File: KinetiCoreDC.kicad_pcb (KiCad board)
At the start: 2 copper layers, 69 parts, among them Q1 BSN20, Q2 BSN20, U1 STM32G070KBT6, U10 MCP1703Ax-330xxDB, U11 WE-TVS-82400102, U2 SN74LVC2G14DBV, U3 DRV8874PWPR, U6 THVD1400D, U7 TLP2310, U8 TLP2310, U9 LTC4365TS8

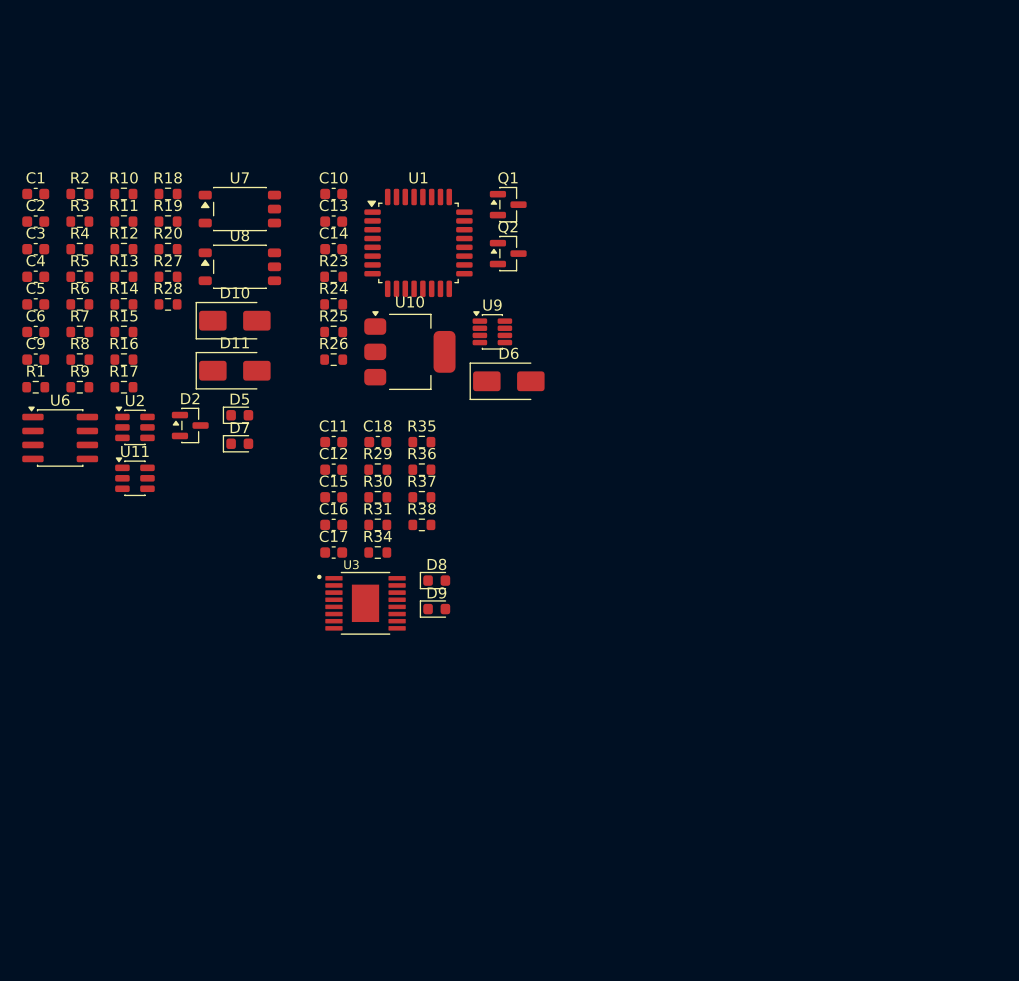
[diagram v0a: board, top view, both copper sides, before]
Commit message: feat : add SMLVN6RGB status LED stage with balanced 3.3V ballast resistors
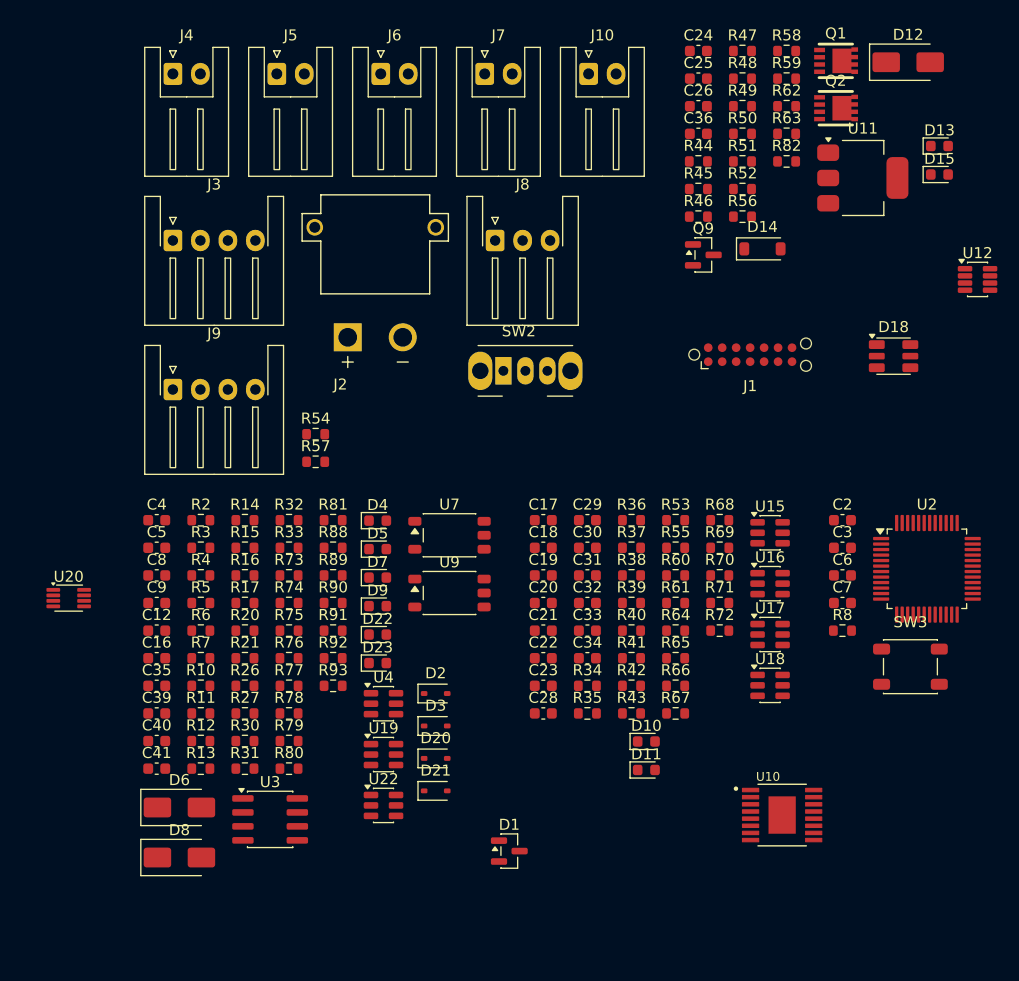
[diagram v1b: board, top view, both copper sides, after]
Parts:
- removed C1, C10, C15: 100nF, Capacitor_SMD:C_0603_1608Metric
- removed C11: 22nF, Capacitor_SMD:C_0603_1608Metric
- removed C13, C14: 1uF, Capacitor_SMD:C_0603_1608Metric
- removed R1, R18, R19, R28: 100R, Resistor_SMD:R_0603_1608Metric
- removed R23: 100k, Resistor_SMD:R_0603_1608Metric
- removed R24: 1.2M, Resistor_SMD:R_0603_1608Metric
- removed R25: 150K, Resistor_SMD:R_0603_1608Metric
- removed R29: 500R, Resistor_SMD:R_0603_1608Metric
- removed R9: 2.2K, Resistor_SMD:R_0603_1608Metric
- removed U1: STM32G070KBT6, Package_QFP:LQFP-32_7x7mm_P0.8mm
- removed U6: THVD1400D, Package_SO:SOIC-8_3.9x4.9mm_P1.27mm
- removed U8: TLP2310, Package_SO:SO-5-6_4.55x3.7mm_P1.27mm
- added C19: 22nF, Capacitor_SMD:C_0603_1608Metric, F.Cu at (160.7, 93.4)
- added C20: 4.7uF, Capacitor_SMD:C_0603_1608Metric, F.Cu at (160.7, 95.9)
- added C21: 22uF, Capacitor_SMD:C_0603_1608Metric, F.Cu at (160.7, 98.5)
- added C22: 100nF, Capacitor_SMD:C_0603_1608Metric, F.Cu at (160.7, 101.0)
- added C23: 10nF, Capacitor_SMD:C_0603_1608Metric, F.Cu at (160.7, 103.5)
- added C24: 1uF, Capacitor_SMD:C_0603_1608Metric, F.Cu at (174.8, 45.8)
- added C25: 1uF, Capacitor_SMD:C_0603_1608Metric, F.Cu at (174.8, 48.3)
- added C26: 100nF, Capacitor_SMD:C_0603_1608Metric, F.Cu at (174.8, 50.8)
- added C28: 1nF, Capacitor_SMD:C_0603_1608Metric, F.Cu at (160.7, 106.0)
- added C29: 1nF, Capacitor_SMD:C_0603_1608Metric, F.Cu at (164.7, 88.4)
- added C30: 100nF, Capacitor_SMD:C_0603_1608Metric, F.Cu at (164.7, 90.9)
- added C31: 100nF, Capacitor_SMD:C_0603_1608Metric, F.Cu at (164.7, 93.4)
- added C32: 100nF, Capacitor_SMD:C_0603_1608Metric, F.Cu at (164.7, 95.9)
- added C33: 100nF, Capacitor_SMD:C_0603_1608Metric, F.Cu at (164.7, 98.5)
- added C34: 100nF, Capacitor_SMD:C_0603_1608Metric, F.Cu at (164.7, 101.0)
- added C35: 220nF, Capacitor_SMD:C_0603_1608Metric, F.Cu at (125.5, 103.5)
- added C36: 1uF, Capacitor_SMD:C_0603_1608Metric, F.Cu at (174.8, 53.3)
- added C39: 10nF, Capacitor_SMD:C_0603_1608Metric, F.Cu at (125.5, 106.0)
- added C40: 10nF, Capacitor_SMD:C_0603_1608Metric, F.Cu at (125.5, 108.5)
- added C41: 100nF, Capacitor_SMD:C_0603_1608Metric, F.Cu at (125.5, 111.0)
- added C7: 100nF, Capacitor_SMD:C_0603_1608Metric, F.Cu at (187.9, 95.9)
- added C8: 100nF, Capacitor_SMD:C_0603_1608Metric, F.Cu at (125.5, 93.4)
- added D1: SM712, Package_TO_SOT_SMD:SOT-23, F.Cu at (157.6, 118.5)
- added D12: SMBJ15CA, Diode_SMD:D_SMA, F.Cu at (193.8, 46.8)
- added D13: LED_Small, LED_SMD:LED_0603_1608Metric, F.Cu at (196.7, 54.4)
- added D14: NSI45020A, Diode_SMD:D_SOD-123, F.Cu at (180.6, 63.7)
- added D15: LED_Small, LED_SMD:LED_0603_1608Metric, F.Cu at (196.7, 57.0)
- added D18: SMLVN6RGB, LED_SMD:LED_ROHM_SMLVN6, F.Cu at (192.5, 73.5)
- added D20: 1N4148WS, Diode_SMD:D_SOD-323, F.Cu at (150.9, 110.1)
- added D21: 1N4148WS, Diode_SMD:D_SOD-323, F.Cu at (150.9, 113.0)
- added D22: LED_Small, LED_SMD:LED_0603_1608Metric, F.Cu at (145.6, 98.8)
- added D23: LED_Small, LED_SMD:LED_0603_1608Metric, F.Cu at (145.6, 101.4)
- added D3: 1N4148WS, Diode_SMD:D_SOD-323, F.Cu at (150.9, 107.1)
- added D4: LED_Small, LED_SMD:LED_0603_1608Metric, F.Cu at (145.6, 88.5)
- added J1: TC2070-IDC-NL, KineticCore:Tag-Connect_TC2070-IDC-FP_2x07_P1.27mm_Vertical, F.Cu at (179.5, 73.4)
- added J10: JST_XH_S2B-A, Connector_JST:JST_XH_S2B-XH-A_1x02_P2.50mm_Horizontal, F.Cu at (164.8, 47.8)
- added J2: XT30PW-M, KineticCore:AMASS_XT30PW-M, F.Cu at (145.4, 61.8)
- added J3: JST_XH_S4B-A, Connector_JST:JST_XH_S4B-XH-A-1_1x04_P2.50mm_Horizontal, F.Cu at (127.0, 63.0)
- added J4: JST_XH_S2B-A, Connector_JST:JST_XH_S2B-XH-A_1x02_P2.50mm_Horizontal, F.Cu at (127.0, 47.8)
- added J5: JST_XH_S2B-A, Connector_JST:JST_XH_S2B-XH-A_1x02_P2.50mm_Horizontal, F.Cu at (136.4, 47.8)
- added J6: JST_XH_S2B-A, Connector_JST:JST_XH_S2B-XH-A_1x02_P2.50mm_Horizontal, F.Cu at (145.9, 47.8)
- added J7: JST_XH_S2B-A, Connector_JST:JST_XH_S2B-XH-A_1x02_P2.50mm_Horizontal, F.Cu at (155.3, 47.8)
- added J8: JST_XH_S3B, Connector_JST:JST_XH_S3B-XH-A-1_1x03_P2.50mm_Horizontal, F.Cu at (156.3, 63.0)
- added J9: JST_XH_S4B-A, Connector_JST:JST_XH_S4B-XH-A-1_1x04_P2.50mm_Horizontal, F.Cu at (127.0, 76.5)
- added Q9: BSS84, Package_TO_SOT_SMD:SOT-23, F.Cu at (175.2, 64.3)
- added R21: 330R, Resistor_SMD:R_0603_1608Metric, F.Cu at (133.5, 101.0)
- added R32: 470R, Resistor_SMD:R_0603_1608Metric, F.Cu at (137.5, 88.4)
- added R33: 22R, Resistor_SMD:R_0603_1608Metric, F.Cu at (137.5, 90.9)
- added R39: 47K, Resistor_SMD:R_0603_1608Metric, F.Cu at (168.7, 95.9)
- added R40: 10K, Resistor_SMD:R_0603_1608Metric, F.Cu at (168.7, 98.5)
- added R41: 2.49K, Resistor_SMD:R_0603_1608Metric, F.Cu at (168.7, 101.0)
- added R42: 22R, Resistor_SMD:R_0603_1608Metric, F.Cu at (168.7, 103.5)
- added R43: 1K, Resistor_SMD:R_0603_1608Metric, F.Cu at (168.7, 106.0)
- added R44: 2.7M, Resistor_SMD:R_0603_1608Metric, F.Cu at (174.8, 55.8)
- added R45: 150k, Resistor_SMD:R_0603_1608Metric, F.Cu at (174.8, 58.3)
- added R46: 100k, Resistor_SMD:R_0603_1608Metric, F.Cu at (174.8, 60.8)
- added R47: 510k, Resistor_SMD:R_0603_1608Metric, F.Cu at (178.8, 45.8)
- added R48: 470R, Resistor_SMD:R_0603_1608Metric, F.Cu at (178.8, 48.3)
- added R49: 10R, Resistor_SMD:R_0603_1608Metric, F.Cu at (178.8, 50.8)
- added R50: 10R, Resistor_SMD:R_0603_1608Metric, F.Cu at (178.8, 53.3)
- added R51: 100R, Resistor_SMD:R_0603_1608Metric, F.Cu at (178.8, 55.8)
- added R52: 100R, Resistor_SMD:R_0603_1608Metric, F.Cu at (178.8, 58.3)
- added R53: 22R, Resistor_SMD:R_0603_1608Metric, F.Cu at (172.7, 88.4)
- added R54: 22R, Resistor_SMD:R_0603_1608Metric, F.Cu at (140.0, 80.6)
- added R55: 1K, Resistor_SMD:R_0603_1608Metric, F.Cu at (172.7, 90.9)
- added R56: 20k, Resistor_SMD:R_0603_1608Metric, F.Cu at (178.8, 60.8)
- added R57: 22R, Resistor_SMD:R_0603_1608Metric, F.Cu at (140.0, 83.1)
- added R58: 10k, Resistor_SMD:R_0603_1608Metric, F.Cu at (182.8, 45.8)
- added R59: 100k, Resistor_SMD:R_0603_1608Metric, F.Cu at (182.8, 48.3)
- added R60: 22R, Resistor_SMD:R_0603_1608Metric, F.Cu at (172.7, 93.4)
- added R61: 22R, Resistor_SMD:R_0603_1608Metric, F.Cu at (172.7, 95.9)
- added R62: 330R, Resistor_SMD:R_0603_1608Metric, F.Cu at (182.8, 50.8)
- added R63: 180R, Resistor_SMD:R_0603_1608Metric, F.Cu at (182.8, 53.3)
- added R64: 1K, Resistor_SMD:R_0603_1608Metric, F.Cu at (172.7, 98.5)
- added R65: 100R, Resistor_SMD:R_0603_1608Metric, F.Cu at (172.7, 101.0)
- added R66: 100R, Resistor_SMD:R_0603_1608Metric, F.Cu at (172.7, 103.5)
- added R67: 2.2K, Resistor_SMD:R_0603_1608Metric, F.Cu at (172.7, 106.0)
- added R68: 2.2K, Resistor_SMD:R_0603_1608Metric, F.Cu at (176.7, 88.4)
- added R69: 10K, Resistor_SMD:R_0603_1608Metric, F.Cu at (176.7, 90.9)
- added R70: 10K, Resistor_SMD:R_0603_1608Metric, F.Cu at (176.7, 93.4)
- added R71: 100R, Resistor_SMD:R_0603_1608Metric, F.Cu at (176.7, 95.9)
- added R72: 100R, Resistor_SMD:R_0603_1608Metric, F.Cu at (176.7, 98.5)
- added R73: 22R, Resistor_SMD:R_0603_1608Metric, F.Cu at (137.5, 93.4)
- added R74: 22R, Resistor_SMD:R_0603_1608Metric, F.Cu at (137.5, 95.9)
- added R75: 10K, Resistor_SMD:R_0603_1608Metric, F.Cu at (137.5, 98.5)
- added R76: 22R, Resistor_SMD:R_0603_1608Metric, F.Cu at (137.5, 101.0)
- added R77: 22R, Resistor_SMD:R_0603_1608Metric, F.Cu at (137.5, 103.5)
- added R78: 10K, Resistor_SMD:R_0603_1608Metric, F.Cu at (137.5, 106.0)
- added R79: 10K, Resistor_SMD:R_0603_1608Metric, F.Cu at (137.5, 108.5)
- added R80: 22R, Resistor_SMD:R_0603_1608Metric, F.Cu at (137.5, 111.0)
- added R81: 22R, Resistor_SMD:R_0603_1608Metric, F.Cu at (141.5, 88.4)
- added R82: 180R, Resistor_SMD:R_0603_1608Metric, F.Cu at (182.8, 55.8)
- added R88: 1K, Resistor_SMD:R_0603_1608Metric, F.Cu at (141.5, 90.9)
- added R89: 1K, Resistor_SMD:R_0603_1608Metric, F.Cu at (141.5, 93.4)
- added R90: 1M, Resistor_SMD:R_0603_1608Metric, F.Cu at (141.5, 95.9)
- added R91: 1M, Resistor_SMD:R_0603_1608Metric, F.Cu at (141.5, 98.5)
- added R92: 470R, Resistor_SMD:R_0603_1608Metric, F.Cu at (141.5, 101.0)
- added R93: 470R, Resistor_SMD:R_0603_1608Metric, F.Cu at (141.5, 103.5)
- added SW2: OS102011MA1Q, Button_Switch_THT:SW_Slide_SPDT_Angled_CK_OS102011MA1Q, F.Cu at (157.0, 74.8)
- added SW3: PTS647, Button_Switch_SMD:SW_SPST_PTS647_Sx38, F.Cu at (194.0, 101.7)
- added U12: LTC4365TS8, Package_TO_SOT_SMD:TSOT-23-8, F.Cu at (200.1, 66.5)
- added U15: WE-TVS-82400102, Package_TO_SOT_SMD:SOT-23-6, F.Cu at (181.3, 89.6)
- added U16: SN74LVC2G14DBV, Package_TO_SOT_SMD:SOT-23-6, F.Cu at (181.3, 94.2)
- added U17: WE-TVS-82400102, Package_TO_SOT_SMD:SOT-23-6, F.Cu at (181.3, 98.8)
- added U18: SN74LVC2G14DBV, Package_TO_SOT_SMD:SOT-23-6, F.Cu at (181.3, 103.4)
- added U19: WE-TVS-82400102, Package_TO_SOT_SMD:SOT-23-6, F.Cu at (146.1, 109.7)
- added U20: 74LVC2G126, Package_SO:VSSOP-8_2.3x2mm_P0.5mm, F.Cu at (117.5, 95.5)
- added U22: SN74LVC2G14DBV, Package_TO_SOT_SMD:SOT-23-6, F.Cu at (146.1, 114.3)
- added U4: SN74LVC2G14DBV, Package_TO_SOT_SMD:SOT-23-6, F.Cu at (146.1, 105.1)
- C17: value 4.7uF -> 100nF
- C18: value 22uF -> 100nF
- C3: value 100nF -> 4.7uF
- C4, C5: value 100nF -> 10nF
- D10, D11: value SMAJ5.0A -> LED_Small; footprint Diode_SMD:D_SMA -> LED_SMD:LED_0603_1608Metric
- D2: value SM712 -> 1N4148WS; footprint Package_TO_SOT_SMD:SOT-23 -> Diode_SMD:D_SOD-323
- D6: value SMAJ15CA -> SMAJ6.0A
- D8: value LED_Small -> SMAJ6.0A; footprint LED_SMD:LED_0603_1608Metric -> Diode_SMD:D_SMA
- Q1, Q2: value BSN20 -> SIS412DN-T1-GE3; footprint Package_TO_SOT_SMD:SOT-23 -> KineticCore:POWERPAK-1212-8
- R10: value 2.2K -> 1M
- R11, R12: value 100R -> 10K
- R15, R16: value 10R -> 22R
- R17: value 120R -> 22R
- R2: value 470R -> 120R
- R20, R31: value 10K -> 330R
- R26: value 150k -> 470R
- R27: value 10K -> 22R
- R30: value 500R -> 330R
- R34: value 2.49K -> 22R
- R35: value 0R -> 2K
- R37: value 16k -> 15K
- R38: value 50k -> 0R
- R4: value 470R -> 1K
- R5: value 1K -> 10R
- R6: value 100R -> 10R
- R7: value 10K -> 1M
- R8: value 10K -> 100R
- U10: value MCP1703Ax-330xxDB -> DRV8874PWPR; footprint Package_TO_SOT_SMD:SOT-223-3_TabPin2 -> KineticCore:SOP65P640X120-17N
- U11: value WE-TVS-82400102 -> MCP1703Ax-330xxDB; footprint Package_TO_SOT_SMD:SOT-23-6 -> Package_TO_SOT_SMD:SOT-223-3_TabPin2
- U2: value SN74LVC2G14DBV -> STM32G070CBTx; footprint Package_TO_SOT_SMD:SOT-23-6 -> Package_QFP:LQFP-48_7x7mm_P0.5mm
- U3: value DRV8874PWPR -> THVD1400D; footprint KineticCore:SOP65P640X120-17N -> Package_SO:SOIC-8_3.9x4.9mm_P1.27mm
- U9: value LTC4365TS8 -> TLP2310; footprint Package_TO_SOT_SMD:TSOT-23-8 -> Package_SO:SO-5-6_4.55x3.7mm_P1.27mm
- moved C2 78.2 mm to (187.9, 88.4)
- moved C3 78.2 mm to (187.9, 90.9)
- moved C6 76.6 mm to (187.9, 93.4)
- moved R8 73.6 mm to (187.9, 98.5)
- moved U2 73.1 mm to (195.5, 92.8)
- moved U11 71.6 mm to (189.7, 57.3)
- moved U10 54.0 mm to (182.4, 115.2)
- moved D10 53.5 mm to (170.0, 108.5)
- moved D11 52.1 mm to (170.0, 111.1)
- moved D6 49.0 mm to (127.6, 114.5)
- moved R12 45.3 mm to (129.5, 108.5)
- moved R11 45.3 mm to (129.5, 106.0)
- moved R13 45.3 mm to (129.5, 111.0)
- moved R10 45.3 mm to (129.5, 103.5)
- moved R27 40.3 mm to (133.5, 106.0)
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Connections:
- C12 pad 1: Net-(U3-VCP) -> +3V3
- C12 pad 2: VM -> GND
- C16 pad 1: VM -> +3V3
- C2 pad 1: +3.3V -> +3V3
- C4 pad 1: +3V3 -> GND
- C4 pad 2: GND -> Net-(D3-A)
- C5 pad 2: Net-(U2-2A) -> Net-(D2-A)
- C6 pad 1: GND -> Net-(U2-NRST)
- C6 pad 2: Net-(U2-1A) -> GND
- D10 pad 1: Net-(D10-A1) -> Net-(D10-K)
- D10 pad 2: /InterfaceSheet/OPTO1_EXT_N -> /DriverMotorSheet/OUTB
- D11 pad 1: Net-(D11-A1) -> /DriverMotorSheet/OUTB
- D11 pad 2: /InterfaceSheet/OPTO2_EXT_N -> Net-(D10-K)
- D2 pad 1: /InterfaceSheet/RS485_A_EXT -> Net-(D2-K)
- D2 pad 2: /InterfaceSheet/RS485_B_EXT -> Net-(D2-A)
- D6 pad 2: GND -> /ConnectorSheet/OPTO1_N
- D8 pad 1: Net-(D8-K) -> Net-(D8-A1)
- D8 pad 2: Net-(D8-A) -> /ConnectorSheet/OPTO2_N
- D9 pad 1: Net-(D8-A) -> GND
- D9 pad 2: Net-(D8-K) -> Net-(D9-A)
- Q1 pad 1: Net-(Q1-G) -> Net-(Q1-S_1)
- Q1 pad 2: Net-(Q1-S) -> Net-(Q1-S_1)
- Q1 pad 3: Net-(D6-A1) -> Net-(Q1-S_1)
- Q2 pad 1: Net-(Q1-G) -> Net-(Q1-S_1)
- Q2 pad 2: Net-(Q1-S) -> Net-(Q1-S_1)
- Q2 pad 3: VM -> Net-(Q1-S_1)
- R10 pad 1: Net-(R10-Pad1) -> Net-(D2-A)
- R11 pad 1: Net-(U2-1Y) -> GND
- R11 pad 2: /InterfaceSheet/TRIG1_MCU -> Net-(U3-DE)
- R12 pad 1: Net-(U2-2Y) -> Net-(U3-RO)
- R12 pad 2: /InterfaceSheet/TRIG2_MCU -> +3V3
- R13 pad 1: Net-(D10-A1) -> Net-(U4-1Y)
- R13 pad 2: Net-(U7-A) -> Net-(D4-A)
- R14 pad 1: Net-(D11-A1) -> Net-(U4-2Y)
- R14 pad 2: Net-(U8-A) -> Net-(D5-A)
- R15 pad 1: /InterfaceSheet/RS485_A_EXT -> Net-(U3-RO)
- R15 pad 2: Net-(U6-A) -> /USART2_RX
- R16 pad 1: /InterfaceSheet/RS485_B_EXT -> Net-(U3-DE)
- R16 pad 2: Net-(U6-B) -> /USART2_DE
- R17 pad 1: /InterfaceSheet/RS485_B_EXT -> Net-(U3-DI)
- R17 pad 2: /InterfaceSheet/RS485_A_EXT -> /USART2_TX
- R2 pad 1: /InterfaceSheet/OPTO1_EXT_P -> /ConnectorSheet/RS485_B
- R2 pad 2: Net-(D10-A1) -> /ConnectorSheet/RS485_A
- R20 pad 1: Net-(U6-RO) -> /ConnectorSheet/OPTO1_P
- R20 pad 2: +3V3 -> Net-(D6-A1)
- R26 pad 1: GND -> Net-(D7-A)
- R26 pad 2: Net-(U9-OV) -> Net-(U7-VO)
- R27 pad 1: GND -> Net-(U7-VO)
- R27 pad 2: Net-(U6-DE) -> /TIM1_CH4
- R3 pad 1: Net-(D5-A) -> /USART2_RX
- R3 pad 2: Net-(U7-VO) -> Net-(D2-K)
- R30 pad 1: /DriverMotorSheet/OUTA -> /ConnectorSheet/OPTO2_P
- R30 pad 2: Net-(D8-A) -> Net-(D8-A1)
- R31 pad 1: /DriverMotorSheet/NFAULT_MCU -> Net-(D8-A1)
- R31 pad 2: +3.3V -> Net-(U9-A)
- R34 pad 1: GND -> /PMODE
- R34 pad 2: /DriverMotorSheet/IPROPI_MCU -> Net-(U10-PMODE)
- R35 pad 1: Net-(U3-IMODE) -> /DriverMotorSheet/OUTA
- R35 pad 2: GND -> Net-(D10-K)
- R36 pad 1: /DriverMotorSheet/PMODE_MCU -> Net-(U10-PMODE)
- R37 pad 1: Net-(U3-VREF) -> Net-(U10-VREF)
- R37 pad 2: +3.3V -> +3V3
- R38 pad 1: Net-(U3-VREF) -> Net-(U10-IMODE)
- R4 pad 1: /InterfaceSheet/OPTO2_EXT_P -> /USART2_TX
- R4 pad 2: Net-(D11-A1) -> Net-(D3-K)
- R5 pad 1: Net-(D7-A) -> /ConnectorSheet/RS485_A
- R5 pad 2: Net-(U8-VO) -> Net-(U3-A)
- R6 pad 1: Net-(U8-VO) -> /ConnectorSheet/RS485_B
- R6 pad 2: /InterfaceSheet/OPTO2_MCU -> Net-(U3-B)
- R7 pad 1: Net-(R7-Pad1) -> Net-(D3-A)
- R7 pad 2: Net-(U2-1A) -> +3V3
- R8 pad 1: Net-(R10-Pad1) -> /NRST
- R8 pad 2: Net-(U2-2A) -> Net-(U2-NRST)
- U10 pad 1: VM -> Net-(U10-EN/IN1)
- U10 pad 2: GND -> Net-(U10-PH/IN2)
- U10 pad 3: +3V3 -> Net-(U10-NSLEEP)
- U11 pad 1: /InterfaceSheet/TRIG1_EXT -> VM
- U11 pad 3: /InterfaceSheet/TRIG2_EXT -> +3V3
- U2 pad 1: Net-(U2-1A) -> unconnected-(U2-PC13-Pad1)
- U2 pad 2: GND -> unconnected-(U2-PC14-Pad2)
- U2 pad 3: Net-(U2-2A) -> unconnected-(U2-PC15-Pad3)
- U2 pad 4: Net-(U2-2Y) -> +3V3
- U2 pad 6: Net-(U2-1Y) -> +3V3
- U3 pad 1: /DriverMotorSheet/EN/IN1_MCU -> Net-(U3-RO)
- U3 pad 2: /DriverMotorSheet/PH/IN2_MCU -> Net-(U3-DE)
- U3 pad 3: /DriverMotorSheet/NSLEEP_MCU -> Net-(U3-DE)
- U3 pad 4: /DriverMotorSheet/NFAULT_MCU -> Net-(U3-DI)
- U3 pad 5: Net-(U3-VREF) -> GND
- U3 pad 6: /DriverMotorSheet/IPROPI_MCU -> Net-(U3-A)
- U3 pad 7: Net-(U3-IMODE) -> Net-(U3-B)
- U3 pad 8: /DriverMotorSheet/OUTA -> +3V3
- U7 pad 3: /InterfaceSheet/OPTO1_EXT_N -> /ConnectorSheet/OPTO1_N
- U7 pad 6: +3.3V -> +3V3
- U9 pad 1: Net-(D6-A1) -> Net-(U9-A)
- U9 pad 3: Net-(U9-OV) -> /ConnectorSheet/OPTO2_N
- U9 pad 6: unconnected-(U9-~{FAULT}-Pad6) -> +3V3

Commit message: feat: add SPI connector and I²c pull up for magnetic encoder
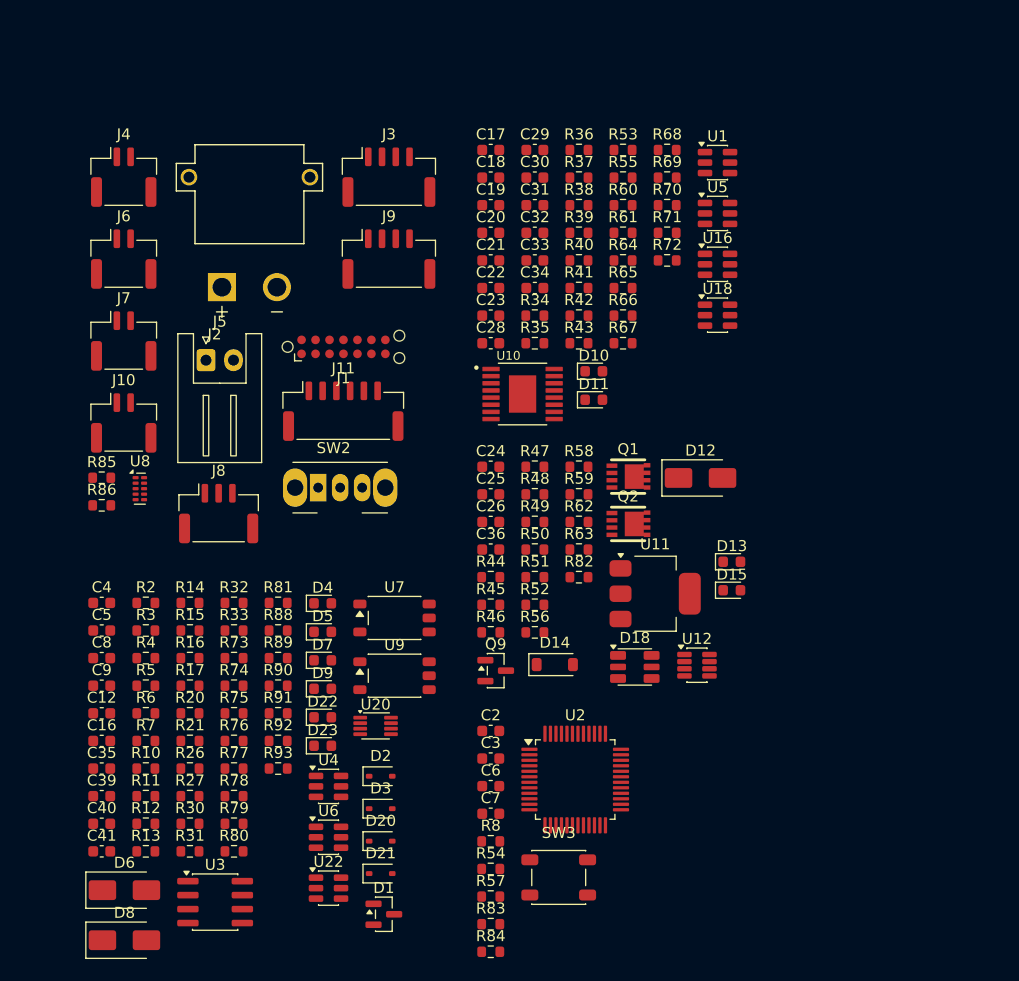
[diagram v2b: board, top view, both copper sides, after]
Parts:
- removed U15, U17, U19: WE-TVS-82400102, Package_TO_SOT_SMD:SOT-23-6
- added J11: Conn_01x06, Connector_JST:JST_GH_SM06B-GHS-TB_1x06-1MP_P1.25mm_Horizontal, F.Cu at (142.5, 78.5)
- added R83: 22R, Resistor_SMD:R_0603_1608Metric, F.Cu at (155.9, 125.1)
- added R84: 22R, Resistor_SMD:R_0603_1608Metric, F.Cu at (155.9, 127.7)
- added R85: 10K, Resistor_SMD:R_0603_1608Metric, F.Cu at (120.5, 84.6)
- added R86: 10K, Resistor_SMD:R_0603_1608Metric, F.Cu at (120.5, 87.1)
- added U1: USBLC6-2SC6, Package_TO_SOT_SMD:SOT-23-6, F.Cu at (176.5, 55.9)
- added U5: USBLC6-2SC6, Package_TO_SOT_SMD:SOT-23-6, F.Cu at (176.5, 60.5)
- added U6: USBLC6-2SC6, Package_TO_SOT_SMD:SOT-23-6, F.Cu at (141.1, 117.2)
- added U8: TPD4E05U06DQA, Package_SON:USON-10_2.5x1.0mm_P0.5mm, F.Cu at (124.0, 85.5)
- J10, J4, J6, J7: value JST_XH_S2B-A -> SM02B-GHS-TB; footprint Connector_JST:JST_XH_S2B-XH-A_1x02_P2.50mm_Horizontal -> Connector_JST:JST_GH_SM02B-GHS-TB_1x02-1MP_P1.25mm_Horizontal
- J3, J9: value JST_XH_S4B-A -> SM04B-GHS-TB; footprint Connector_JST:JST_XH_S4B-XH-A-1_1x04_P2.50mm_Horizontal -> Connector_JST:JST_GH_SM04B-GHS-TB_1x04-1MP_P1.25mm_Horizontal
- J5: value JST_XH_S2B-A -> BM02B-GHS-TBT
- J8: value JST_XH_S3B -> SM03B-GHS-TB; footprint Connector_JST:JST_XH_S3B-XH-A-1_1x03_P2.50mm_Horizontal -> Connector_JST:JST_GH_SM03B-GHS-TB_1x03-1MP_P1.25mm_Horizontal
- moved J10 52.9 mm to (122.5, 79.6)
- moved U10 45.0 mm to (158.8, 76.9)
- moved U12 43.4 mm to (174.6, 101.6)
- moved R54 42.6 mm to (155.9, 120.1)
- moved R57 42.6 mm to (155.9, 122.6)
- moved D12 42.3 mm to (174.9, 84.6)
- moved D14 42.3 mm to (161.7, 101.5)
- moved D13 42.3 mm to (177.8, 92.2)
- moved C24 42.3 mm to (155.9, 83.6)
- moved C26 42.3 mm to (155.9, 88.6)
- moved D15 42.3 mm to (177.8, 94.8)
- moved Q9 42.3 mm to (156.3, 102.1)
- moved R45 42.3 mm to (155.9, 96.1)
- moved R47 42.3 mm to (159.9, 83.6)
- moved R49 42.3 mm to (159.9, 88.6)
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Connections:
- J3 pad 1: Net-(J3-Pin_1) -> +3V3
- J9 pad 1: Net-(J9-Pin_1) -> +3V3
- R54 pad 1: Net-(J3-Pin_1) -> /ConnectorSheet/MISO_MCU
- R54 pad 2: +3V3 -> /SPI2_MISO
- R57 pad 1: Net-(J9-Pin_1) -> /ConnectorSheet/MOSI_MCU
- R57 pad 2: +3V3 -> /SPI2_MOSI
